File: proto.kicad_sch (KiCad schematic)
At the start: 1 part, among them U2 MCP2515_Breakout

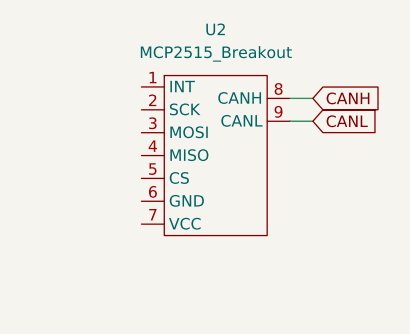
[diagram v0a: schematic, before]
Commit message: Boards should be placed correctly now
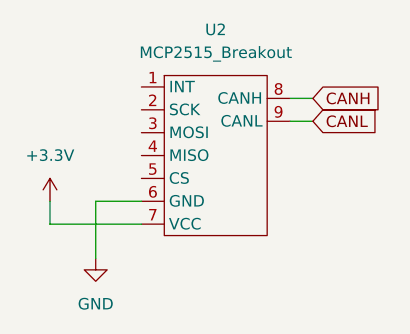
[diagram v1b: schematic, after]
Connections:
- net GND: now reaches U2.6 (GND)
- net +3.3V: now reaches U2.7 (VCC)
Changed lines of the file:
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@@
+    (stroke (width 0) (type default) (color 0 0 0 0))
+  )
+  (wire (pts (xy 22.86 40.64) (xy 33.02 40.64))
+    (stroke (width 0) (type default) (color 0 0 0 0))
+  )
+  (wire (pts (xy 27.94 38.1) (xy 27.94 44.45))
+    (stroke (width 0) (type default) (color 0 0 0 0))
+  )
+  (wire (pts (xy 22.86 38.1) (xy 22.86 40.64))
+    (stroke (width 0) (type default) (color 0 0 0 0))
+  )
+  (wire (pts (xy 33.02 38.1) (xy 27.94 38.1))
     (stroke (width 0) (type default) (color 0 0 0 0))
   )
@@
     (pin "9")
   )
+  (symbol (lib_id "power:GND") (at 27.94 44.45 0) (unit 1)
+    (in_bom yes) (on_board yes) (fields_autoplaced)
+    (property "Reference" "#PWR0142" (id 0) (at 27.94 50.8 0)
+      (effects (font (size 1.27 1.27)) hide)
+    )
+    (property "Value" "GND" (id 1) (at 27.94 49.53 0))
+    (property "Footprint" "" (id 2) (at 27.94 44.45 0)
+      (effects (font (size 1.27 1.27)) hide)
+    )
+    (property "Datasheet" "" (id 3) (at 27.94 44.45 0)
+      (effects (font (size 1.27 1.27)) hide)
+    )
+    (pin "1")
+  )
+  (symbol (lib_id "power:+3.3V") (at 22.86 38.1 0) (unit 1)
+    (in_bom yes) (on_board yes) (fields_autoplaced)
+    (property "Reference" "#PWR0141" (id 0) (at 22.86 41.91 0)
+      (effects (font (size 1.27 1.27)) hide)
+    )
+    (property "Value" "+3.3V" (id 1) (at 22.86 33.02 0))
+    (property "Footprint" "" (id 2) (at 22.86 38.1 0)
+      (effects (font (size 1.27 1.27)) hide)
+    )
+    (property "Datasheet" "" (id 3) (at 22.86 38.1 0)
+      (effects (font (size 1.27 1.27)) hide)
+    )
+    (pin "1")
+  )
 )

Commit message: More changes
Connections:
- net CAN_INT: now reaches U2.1 (INT)
- net SCK: now reaches U2.2 (SCK)
- net MOSI: now reaches U2.3 (MOSI)
- net MISO: now reaches U2.4 (MISO)
- net CAN_CS: now reaches U2.5 (CS)
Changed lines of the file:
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@@
     (stroke (width 0) (type default) (color 0 0 0 0))
+  )
+  (global_label "CAN_CS" (shape input) (at 33.02 35.56 180) (fields_autoplaced)
+    (effects (font (size 1.27 1.27)) (justify right))
+    (property "Intersheet References" "${INTERSHEET_REFS}" (id 0) (at 23.5596 35.4806 0)
+      (effects (font (size 1.27 1.27)) (justify right) hide)
+    )
   )
   (global_label "CANL" (shape input) (at 52.07 29.21 0) (fields_autoplaced)
@@
     )
   )
+  (global_label "MISO" (shape input) (at 33.02 33.02 180) (fields_autoplaced)
+    (effects (font (size 1.27 1.27)) (justify right))
+    (property "Intersheet References" "${INTERSHEET_REFS}" (id 0) (at 26.0996 32.9406 0)
+      (effects (font (size 1.27 1.27)) (justify right) hide)
+    )
+  )
+  (global_label "SCK" (shape input) (at 33.02 27.94 180) (fields_autoplaced)
+    (effects (font (size 1.27 1.27)) (justify right))
+    (property "Intersheet References" "${INTERSHEET_REFS}" (id 0) (at 26.9463 28.0194 0)
+      (effects (font (size 1.27 1.27)) (justify right) hide)
+    )
+  )
+  (global_label "CAN_INT" (shape input) (at 33.02 25.4 180) (fields_autoplaced)
+    (effects (font (size 1.27 1.27)) (justify right))
+    (property "Intersheet References" "${INTERSHEET_REFS}" (id 0) (at 23.1363 25.3206 0)
+      (effects (font (size 1.27 1.27)) (justify right) hide)
+    )
+  )
+  (global_label "MOSI" (shape input) (at 33.02 30.48 180) (fields_autoplaced)
+    (effects (font (size 1.27 1.27)) (justify right))
+    (property "Intersheet References" "${INTERSHEET_REFS}" (id 0) (at 26.0996 30.4006 0)
+      (effects (font (size 1.27 1.27)) (justify right) hide)
+    )
+  )

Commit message: Add stuff
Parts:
- added U4: TCAN330, Package_TO_SOT_SMD:SOT-23-8, symbol Interface_CAN_LIN:TCAN330
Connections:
- net +3.3V: now also U4.3 (VCC)
- net CANH: now also U4.7 (CANH)
- net CANL: now also U4.6 (CANL)
- net GND: now also U4.2 (GND)
- new net MCU_CANRX: U4.4 (RXD)
- new net MCU_CANTX: U4.1 (TXD)
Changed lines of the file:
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@@
+    )
+  )
+  (global_label "CANH" (shape input) (at 101.6 27.94 0) (fields_autoplaced)
+    (effects (font (size 1.27 1.27)) (justify left))
+    (property "Intersheet References" "${INTERSHEET_REFS}" (id 0) (at 108.9437 27.8606 0)
+      (effects (font (size 1.27 1.27)) (justify left) hide)
     )
   )
@@
     (property "Intersheet References" "${INTERSHEET_REFS}" (id 0) (at 59.4137 26.5906 0)
       (effects (font (size 1.27 1.27)) (justify left) hide)
+    )
+  )
+  (global_label "MCU_CANTX" (shape input) (at 76.2 25.4 180) (fields_autoplaced)
+    (effects (font (size 1.27 1.27)) (justify right))
+    (property "Intersheet References" "${INTERSHEET_REFS}" (id 0) (at 62.9901 25.3206 0)
+      (effects (font (size 1.27 1.27)) (justify right) hide)
     )
   )
@@
     )
   )
+  (global_label "MCU_CANRX" (shape input) (at 76.2 27.94 180) (fields_autoplaced)
+    (effects (font (size 1.27 1.27)) (justify right))
+    (property "Intersheet References" "${INTERSHEET_REFS}" (id 0) (at 62.6877 27.8606 0)
+      (effects (font (size 1.27 1.27)) (justify right) hide)
+    )
+  )
   (global_label "MOSI" (shape input) (at 33.02 30.48 180) (fields_autoplaced)
     (effects (font (size 1.27 1.27)) (justify right))
     (property "Intersheet References" "${INTERSHEET_REFS}" (id 0) (at 26.0996 30.4006 0)
       (effects (font (size 1.27 1.27)) (justify right) hide)
+    )
+  )
+  (global_label "CANL" (shape input) (at 101.6 33.02 0) (fields_autoplaced)
+    (effects (font (size 1.27 1.27)) (justify left))
+    (property "Intersheet References" "${INTERSHEET_REFS}" (id 0) (at 108.6413 32.9406 0)
+      (effects (font (size 1.27 1.27)) (justify left) hide)
     )
   )
@@
     (pin "1")
   )
+  (symbol (lib_id "Interface_CAN_LIN:TCAN330") (at 88.9 30.48 0) (unit 1)
+    (in_bom yes) (on_board yes) (fields_autoplaced)
+    (property "Reference" "U4" (id 0) (at 90.9194 17.78 0)
+      (effects (font (size 1.27 1.27)) (justify left))
+    )
+    (property "Value" "TCAN330" (id 1) (at 90.9194 20.32 0)
+      (effects (font (size 1.27 1.27)) (justify left))
+    )
+    (property "Footprint" "Package_TO_SOT_SMD:SOT-23-8" (id 2) (at 88.9 43.18 0)
+      (effects (font (size 1.27 1.27) italic) hide)
+    )
+    (property "Datasheet" "http://www.ti.com/lit/ds/symlink/tcan337.pdf" (id 3) (at 88.9 30.48 0)
+      (effects (font (size 1.27 1.27)) hide)
+    )
+    (property "JLCPCB" "C2877587" (id 4) (at 88.9 30.48 0)
+      (effects (font (size 1.27 1.27)) hide)
+    )
+    (pin "1")
+    (pin "2")
+    (pin "3")
+    (pin "4")
+    (pin "5")
+    (pin "6")
+    (pin "7")
+    (pin "8")
+  )
+  (symbol (lib_id "power:GND") (at 88.9 40.64 0) (unit 1)
+    (in_bom yes) (on_board yes) (fields_autoplaced)
+    (property "Reference" "#PWR0161" (id 0) (at 88.9 46.99 0)
+      (effects (font (size 1.27 1.27)) hide)
+    )
+    (property "Value" "GND" (id 1) (at 88.9 45.72 0))
+    (property "Footprint" "" (id 2) (at 88.9 40.64 0)
+      (effects (font (size 1.27 1.27)) hide)
+    )
+    (property "Datasheet" "" (id 3) (at 88.9 40.64 0)
+      (effects (font (size 1.27 1.27)) hide)
+    )
+    (pin "1")
+  )
   (symbol (lib_id "power:+3.3V") (at 22.86 38.1 0) (unit 1)
     (in_bom yes) (on_board yes) (fields_autoplaced)
@@
       (effects (font (size 1.27 1.27)) hide)
     )
+    (pin "1")
+  )
+  (symbol (lib_id "power:+3.3V") (at 88.9 20.32 0) (unit 1)
+    (in_bom yes) (on_board yes) (fields_autoplaced)
+    (property "Reference" "#PWR0162" (id 0) (at 88.9 24.13 0)
+      (effects (font (size 1.27 1.27)) hide)
+    )
+    (property "Value" "+3.3V" (id 1) (at 88.9 15.24 0))
+    (property "Footprint" "" (id 2) (at 88.9 20.32 0)
+      (effects (font (size 1.27 1.27)) hide)
+    )
+    (property "Datasheet" "" (id 3) (at 88.9 20.32 0)
+      (effects (font (size 1.27 1.27)) hide)
+    )
